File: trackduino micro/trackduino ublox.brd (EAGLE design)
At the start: 52.6 x 22.3 mm, 28 parts, among them IC1 74AHC1G125DBV, IC2 74AHC1G125DBV, IC3 74AHC1G125DBV, U1 ATMEGA168

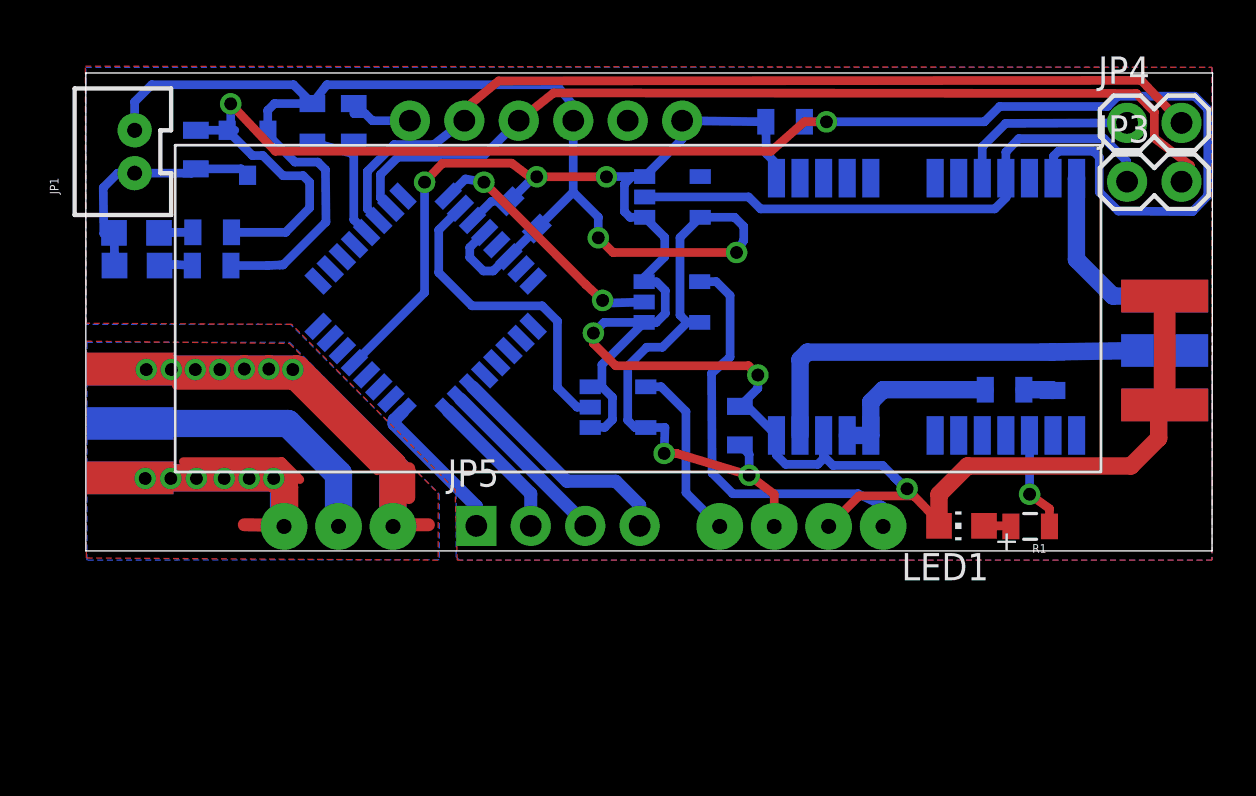
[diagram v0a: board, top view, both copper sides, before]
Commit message: reset switch
added a reset switch and improved RF ground fill.
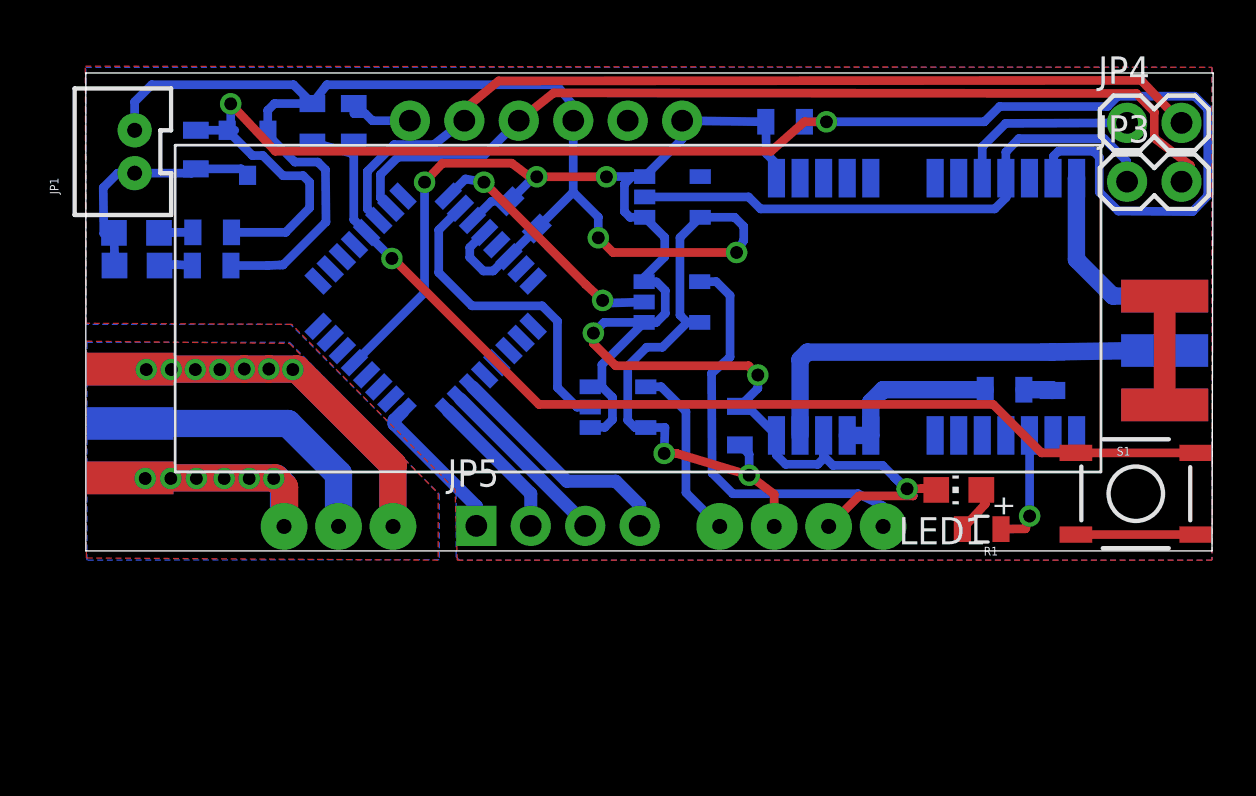
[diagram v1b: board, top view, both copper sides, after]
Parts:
- added S1: TAC_SWITCHSMD, SparkFun-Electromechanical:TACTILE-SWITCH-SMD
- moved R1 2.26 mm to (88.4, 58.5)
- moved LED1 1.68 mm to (87.4, 60.3)
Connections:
- net GND: now also S1.3, S1.4
- net N$9: now also S1.1, S1.2
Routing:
- net N$9: track 6.93 -> 49.9 mm, vias 0 -> 1
- net N$11: track 11.0 -> 0.00 mm
- net GND: track 178.8 -> 169.4 mm
- net N$10: track 5.78 -> 0.00 mm
- net N$14: track 1.93 -> 0.00 mm
- net N$15: track 1.55 -> 0.00 mm
- net N$16: track 1.35 -> 0.00 mm
- net N$3: track 1.26 -> 2.27 mm
- net N$2: track 4.72 -> 5.53 mm
- removed copper zone on layer 1, net RF
- removed copper zone on layer 16, net RF
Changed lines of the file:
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@@
 <plain>
 <wire x1="46.6598" y1="57.4548" x2="99.1872" y2="57.4548" width="0" layer="20"/>
-<wire x1="99.1872" y1="57.4548" x2="99.2126" y2="79.746" width="0" layer="20"/>
-<wire x1="99.2126" y1="79.746" x2="46.6598" y2="79.746" width="0" layer="20"/>
+<wire x1="99.1872" y1="57.4548" x2="99.238" y2="79.746" width="0" layer="20"/>
+<wire x1="99.238" y1="79.746" x2="46.6598" y2="79.746" width="0" layer="20"/>
 <wire x1="46.6598" y1="79.746" x2="46.6598" y2="57.4548" width="0" layer="20"/>
 </plain>
@@
 <element name="JP1" library="SparkFun-Connectors" package="JST-2-PTH-VERT" value="M02JST-PTH-VERT" x="48.387" y="76.073" rot="R90"/>
 <element name="J$1" library="SparkFun-Connectors" package="SMA-EDGE" value="SMA_EDGE" x="48.7172" y="60.8584" rot="MR90"/>
-<element name="R1" library="SparkFun-Resistors" package="0805" value="" x="90.7034" y="58.5978" rot="R180"/>
-<element name="LED1" library="adafruit" package="CHIP-LED0805" value="" x="87.503" y="58.6232" rot="R90"/>
+<element name="R1" library="SparkFun-Resistors" package="0805" value="" x="88.4428" y="58.4708" rot="R180"/>
+<element name="LED1" library="adafruit" package="CHIP-LED0805" value="" x="87.376" y="60.2996" rot="R90"/>
 <element name="R2" library="SparkFun-Resistors" package="0805" value="" x="89.5096" y="64.9732" rot="MR180"/>
 <element name="L1" library="SparkFun-Passives" package="0805" value="" x="91.7448" y="65.8368" rot="MR90"/>
@@
 <element name="JP4" library="SparkFun-Connectors" package="1X02" value="M02PTH" x="95.2246" y="77.4192"/>
 <element name="JP5" library="SparkFun-Connectors" package="1X04_NO_SILK" value="" x="64.8716" y="58.6232"/>
+<element name="S1" library="SparkFun-Electromechanical" package="TACTILE-SWITCH-SMD" value="TAC_SWITCHSMD" x="95.631" y="60.1218">
+<attribute name="PROD_ID" value="SWCH-08247" x="95.631" y="60.1218" size="1.778" layer="27" display="off"/>
+</element>
 </elements>
 <signals>
@@
 <wire x1="78.867" y1="75.5142" x2="78.867" y2="74.8444" width="0.4064" layer="16"/>
 <wire x1="78.867" y1="74.8444" x2="78.871" y2="74.8404" width="0.4064" layer="16"/>
-<wire x1="86.453" y1="58.6232" x2="86.453" y2="58.8096" width="0.4064" layer="1"/>
-<wire x1="86.453" y1="58.8096" x2="84.963" y2="60.3504" width="0.4064" layer="1"/>
+<wire x1="86.326" y1="60.2996" x2="85.6656" y2="60.359" width="0.4064" layer="1"/>
+<wire x1="85.6656" y1="60.359" x2="84.963" y2="60.3504" width="0.4064" layer="1"/>
 <wire x1="84.963" y1="60.3504" x2="85.2424" y2="60.0202" width="0.4064" layer="1"/>
 <wire x1="85.2424" y1="60.0202" x2="82.7278" y2="60.0202" width="0.4064" layer="1"/>
@@
 <wire x1="92.8624" y1="71.0438" x2="92.8624" y2="74.8318" width="0.8128" layer="16"/>
 <wire x1="92.8624" y1="74.8318" x2="92.871" y2="74.8404" width="0.8128" layer="16"/>
-<wire x1="86.453" y1="58.8096" x2="86.453" y2="60.0878" width="0.8128" layer="1"/>
-<wire x1="86.453" y1="60.0878" x2="87.7824" y2="61.4172" width="0.8128" layer="1"/>
-<wire x1="87.7824" y1="61.4172" x2="95.4024" y2="61.4172" width="0.8128" layer="1"/>
-<wire x1="95.4024" y1="61.4172" x2="96.6978" y2="62.7126" width="0.8128" layer="1"/>
-<wire x1="96.6978" y1="62.7126" x2="96.6978" y2="64.1604" width="0.8128" layer="1"/>
 <polygon width="0.4064" layer="1">
 <vertex x="46.6344" y="80.0608"/>
@@
 <via x="54.0512" y="65.9384" extent="1-16" drill="0.6" shape="square"/>
 <via x="55.1942" y="65.9384" extent="1-16" drill="0.6" shape="square"/>
-<wire x1="59.19123125" y1="66.233915625" x2="56.515" y2="65.9384" width="0" layer="19" extent="16-16"/>
+<contactref element="S1" pad="4"/>
+<contactref element="S1" pad="3"/>
+<wire x1="92.837" y1="58.2168" x2="98.425" y2="58.2168" width="0.4064" layer="1"/>
+<polygon width="0.4064" layer="1" pour="hatch" orphans="yes">
+<vertex x="46.6852" y="67.2338"/>
+<vertex x="56.1594" y="67.1322"/>
+<vertex x="63.0936" y="60.1472"/>
+<vertex x="63.0936" y="57.023"/>
+<vertex x="46.6852" y="57.1246"/>
+</polygon>
+<polygon width="0.3048" layer="16" pour="hatch" orphans="yes">
+<vertex x="46.7106" y="67.183"/>
+<vertex x="56.1594" y="67.183"/>
+<vertex x="63.1444" y="60.0964"/>
+<vertex x="63.1444" y="57.0484"/>
+<vertex x="46.7106" y="57.023"/>
+</polygon>
+<wire x1="96.6978" y1="64.1604" x2="98.425" y2="58.2168" width="0" layer="19" extent="1-1"/>
+<wire x1="96.9772" y1="64.262" x2="96.9772" y2="64.262" width="0" layer="19" extent="1-16"/>
+<wire x1="56.515" y1="65.9384" x2="59.19123125" y2="66.233915625" width="0" layer="19" extent="16-16"/>
 <wire x1="55.9562" y1="58.6232" x2="60.9854" y2="58.5978" width="0" layer="19" extent="1-1"/>
 <wire x1="48.7172" y1="60.8584" x2="48.7172" y2="60.8584" width="0" layer="19" extent="1-16"/>
@@
 <contactref element="U$1" pad="3_TIMEPULSE"/>
 <contactref element="R1" pad="1"/>
-<wire x1="91.6034" y1="58.5978" x2="91.6034" y2="59.425" width="0.4064" layer="1"/>
-<wire x1="91.6034" y1="59.425" x2="90.678" y2="60.0964" width="0.4064" layer="1"/>
-<via x="90.678" y="60.0964" extent="1-16" drill="0.6" shape="square"/>
-<wire x1="90.678" y1="60.0964" x2="90.678" y2="62.8334" width="0.4064" layer="16"/>
+<wire x1="89.3428" y1="58.4708" x2="90.4858" y2="58.4852" width="0.4064" layer="1"/>
+<wire x1="90.4858" y1="58.4852" x2="90.678" y2="59.0804" width="0.4064" layer="1"/>
+<via x="90.678" y="59.0804" extent="1-16" drill="0.6" shape="square"/>
+<wire x1="90.678" y1="59.0804" x2="90.678" y2="62.8334" width="0.4064" layer="16"/>
 <wire x1="90.678" y1="62.8334" x2="90.671" y2="62.8404" width="0.4064" layer="16"/>
 </signal>
@@
 <contactref element="R1" pad="2"/>
 <contactref element="LED1" pad="A"/>
-<wire x1="88.553" y1="58.6232" x2="89.778" y2="58.6232" width="0.4064" layer="1"/>
-<wire x1="89.778" y1="58.6232" x2="89.8034" y2="58.5978" width="0.4064" layer="1"/>
+<wire x1="88.426" y1="60.2996" x2="88.6096" y2="59.6392" width="0.4064" layer="1"/>
+<wire x1="88.6096" y1="59.6392" x2="87.5428" y2="58.4708" width="0.4064" layer="1"/>
 </signal>
 <signal name="N$4">
@@
 <wire x1="59.1566" y1="76.5192" x2="59.0804" y2="75.9858" width="0.4064" layer="16"/>
 <wire x1="59.0804" y1="75.9858" x2="57.2262" y2="76.5192" width="0.4064" layer="16"/>
+<contactref element="S1" pad="1"/>
+<contactref element="S1" pad="2"/>
+<wire x1="59.75691875" y1="72.30456875" x2="59.75691875" y2="72.27228125" width="0.4064" layer="16"/>
+<wire x1="59.75691875" y1="72.27228125" x2="60.9346" y2="71.0946" width="0.4064" layer="16"/>
+<via x="60.9346" y="71.0946" extent="1-16" drill="0.6" shape="square"/>
+<wire x1="60.9346" y1="71.0946" x2="60.9854" y2="71.0946" width="0.4064" layer="1"/>
+<wire x1="60.9854" y1="71.0946" x2="67.7926" y2="64.2874" width="0.4064" layer="1"/>
+<wire x1="67.7926" y1="64.2874" x2="88.9762" y2="64.2874" width="0.4064" layer="1"/>
+<wire x1="88.9762" y1="64.2874" x2="91.2368" y2="62.0268" width="0.4064" layer="1"/>
+<wire x1="91.2368" y1="62.0268" x2="92.837" y2="62.0268" width="0.4064" layer="1"/>
+<wire x1="92.837" y1="62.0268" x2="98.425" y2="62.0268" width="0.4064" layer="1"/>
 </signal>
 <signal name="RXO">
@@
 <via x="49.4284" y="60.833" extent="1-16" drill="0.6" shape="square"/>
 </signal>
-<signal name="RF">
-<polygon width="0.4064" layer="1">
-<vertex x="46.6852" y="67.2338"/>
-<vertex x="56.1594" y="67.1322"/>
-<vertex x="63.0936" y="60.1472"/>
-<vertex x="63.0936" y="57.023"/>
-<vertex x="46.6852" y="57.1246"/>
-</polygon>
-<polygon width="0.4064" layer="16">
-<vertex x="46.7106" y="67.183"/>
-<vertex x="56.1594" y="67.183"/>
-<vertex x="63.1444" y="60.0964"/>
-<vertex x="63.1444" y="57.0484"/>
-<vertex x="46.7106" y="57.023"/>
-</polygon>
-</signal>
-<signal name="N$14">
-<wire x1="54.0512" y1="58.674" x2="55.9816" y2="58.6486" width="0.6096" layer="1"/>
-</signal>
 <signal name="N$15">
-<wire x1="61.087" y1="58.674" x2="62.6364" y2="58.674" width="0.6096" layer="1"/>
 </signal>
 <signal name="N$16">
-<wire x1="61.722" y1="61.2902" x2="61.722" y2="59.944" width="0.6096" layer="1"/>
 </signal>
 <signal name="N$17">
@@
 </signal>
 <signal name="N$10">
-<wire x1="51.2064" y1="61.6204" x2="55.8038" y2="61.6204" width="0.4064" layer="1"/>
-<wire x1="55.8038" y1="61.6204" x2="56.642" y2="60.7822" width="0.4064" layer="1"/>
 </signal>
 <signal name="N$11">
-<wire x1="50.8762" y1="65.1764" x2="56.261" y2="65.1764" width="0.4064" layer="1"/>
-<wire x1="56.261" y1="65.1764" x2="60.2488" y2="61.1886" width="0.4064" layer="1"/>
 </signal>
 </signals>

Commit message: fixed missing vcc / ground connections
missed AVCC and AGND
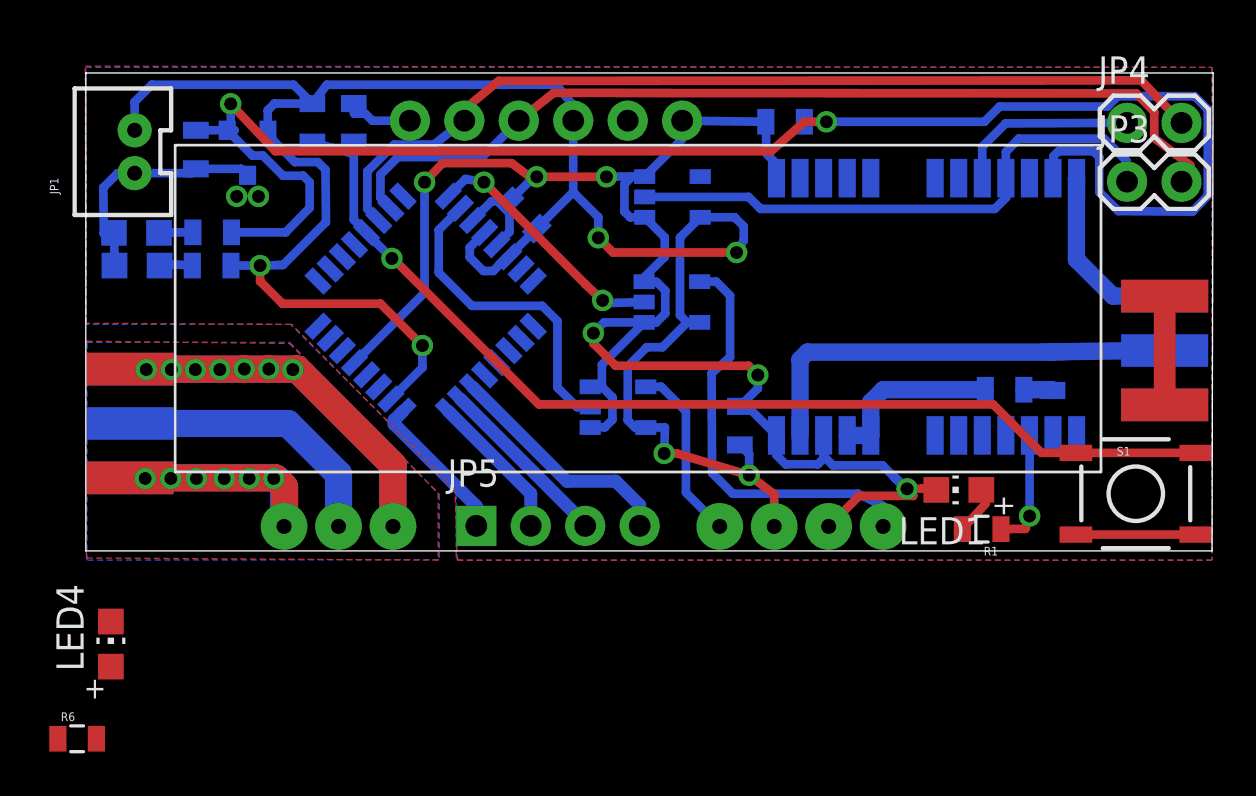
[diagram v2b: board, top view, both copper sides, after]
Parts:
- added LED4: (no value), adafruit:CHIP-LED0805
- added R6: (no value), SparkFun-Resistors:0805
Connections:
- new net N$14: LED4.A, R6.1
- net GND: now also LED4.C, U1.5
- net VCC: now also U1.18
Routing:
- net VCC: track 86.7 -> 99.3 mm, vias 4 -> 6
- net GND: track 169.4 -> 171.6 mm
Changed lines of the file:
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@@
 <attribute name="PROD_ID" value="SWCH-08247" x="95.631" y="60.1218" size="1.778" layer="27" display="off"/>
 </element>
+<element name="LED4" library="adafruit" package="CHIP-LED0805" value="" x="47.8282" y="53.1114"/>
+<element name="R6" library="SparkFun-Resistors" package="0805" value="" x="46.2534" y="48.6918"/>
 </elements>
 <signals>
@@
 <vertex x="46.7106" y="57.023"/>
 </polygon>
+<contactref element="LED4" pad="C"/>
+<contactref element="U1" pad="5"/>
+<wire x1="65.827571875" y1="71.73888125" x2="66.41960625" y2="72.330915625" width="0.4064" layer="16"/>
+<wire x1="66.41960625" y1="72.330915625" x2="66.41960625" y2="73.76299375" width="0.4064" layer="16"/>
 <wire x1="96.6978" y1="64.1604" x2="98.425" y2="58.2168" width="0" layer="19" extent="1-1"/>
 <wire x1="96.9772" y1="64.262" x2="96.9772" y2="64.262" width="0" layer="19" extent="1-16"/>
@@
 <wire x1="55.9562" y1="58.6232" x2="60.9854" y2="58.5978" width="0" layer="19" extent="1-1"/>
 <wire x1="48.7172" y1="60.8584" x2="48.7172" y2="60.8584" width="0" layer="19" extent="1-16"/>
+<wire x1="47.8282" y1="54.1614" x2="48.7172" y2="60.8584" width="0" layer="19" extent="1-1"/>
 </signal>
 <signal name="VCC">
@@
 <wire x1="55.8546" y1="70.7898" x2="55.7022" y2="70.7898" width="0.4064" layer="16"/>
 <wire x1="55.7022" y1="70.7898" x2="55.1434" y2="70.7644" width="0.4064" layer="16"/>
-<wire x1="55.1434" y1="70.7644" x2="53.4272" y2="70.7644" width="0.4064" layer="16"/>
+<wire x1="55.1434" y1="70.7644" x2="54.7878" y2="70.7644" width="0.4064" layer="16"/>
+<contactref element="U1" pad="18"/>
+<wire x1="54.737" y1="70.7644" x2="53.4272" y2="70.7644" width="0.4064" layer="16"/>
+<wire x1="60.8882875" y1="64.536859375" x2="62.357" y2="66.005571875" width="0.4064" layer="16"/>
+<wire x1="62.357" y1="66.005571875" x2="62.357" y2="67.0306" width="0.4064" layer="16"/>
+<via x="62.357" y="67.0306" extent="1-16" drill="0.6" shape="square"/>
+<wire x1="62.357" y1="67.0306" x2="60.4012" y2="68.9864" width="0.4064" layer="1"/>
+<wire x1="60.4012" y1="68.9864" x2="55.8292" y2="68.9864" width="0.4064" layer="1"/>
+<wire x1="55.8292" y1="68.9864" x2="54.7878" y2="70.0278" width="0.4064" layer="1"/>
+<wire x1="54.7878" y1="70.0278" x2="54.7878" y2="70.7644" width="0.4064" layer="1"/>
+<via x="54.7878" y="70.7644" extent="1-16" drill="0.6" shape="square"/>
+<wire x1="54.7878" y1="70.7644" x2="54.737" y2="70.7644" width="0.4064" layer="16"/>
 </signal>
 <signal name="EN-5V">
@@
 <signal name="N$11">
 </signal>
+<signal name="N$14">
+<contactref element="LED4" pad="A"/>
+<contactref element="R6" pad="1"/>
+<wire x1="45.3534" y1="48.6918" x2="47.8282" y2="52.0614" width="0" layer="19" extent="1-1"/>
+</signal>
+<signal name="N$26">
+<via x="53.6956" y="73.9902" extent="1-16" drill="0.6" shape="square"/>
+</signal>
+<signal name="N$27">
+<via x="54.7116" y="73.9902" extent="1-16" drill="0.6" shape="square"/>
+</signal>
 </signals>
